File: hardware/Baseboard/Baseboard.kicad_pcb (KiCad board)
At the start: 2 copper layers, 160 x 160 mm, 77 parts, among them IC1 74HC00, IC10 W65C22, IC11 74HC148, IC12 74HC273, IC2 W65C02, IC3 74HC138, IC4 SYSTEM ROM, IC5 RAM, IC6 W65C22, IC7 W65C51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

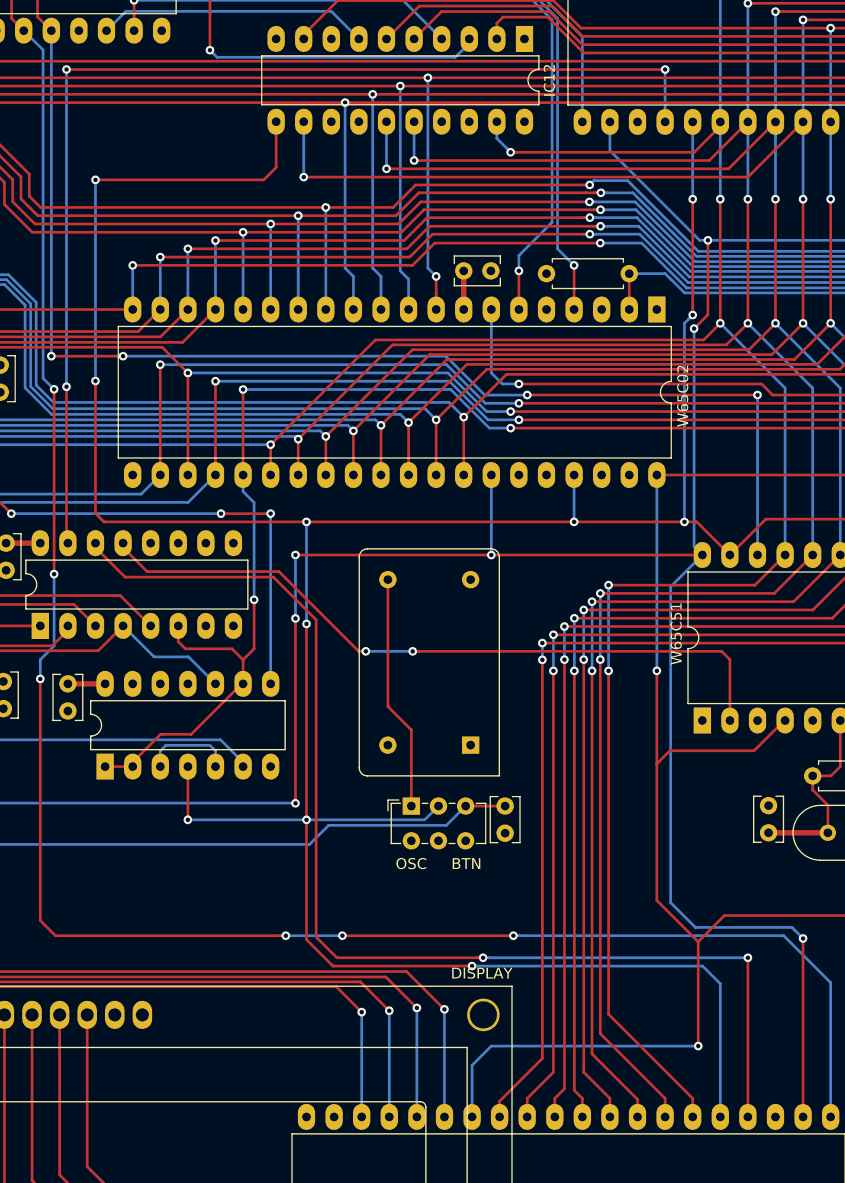
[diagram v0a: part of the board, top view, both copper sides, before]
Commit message: Move CS signals for peripheral devices to not(CS) pins
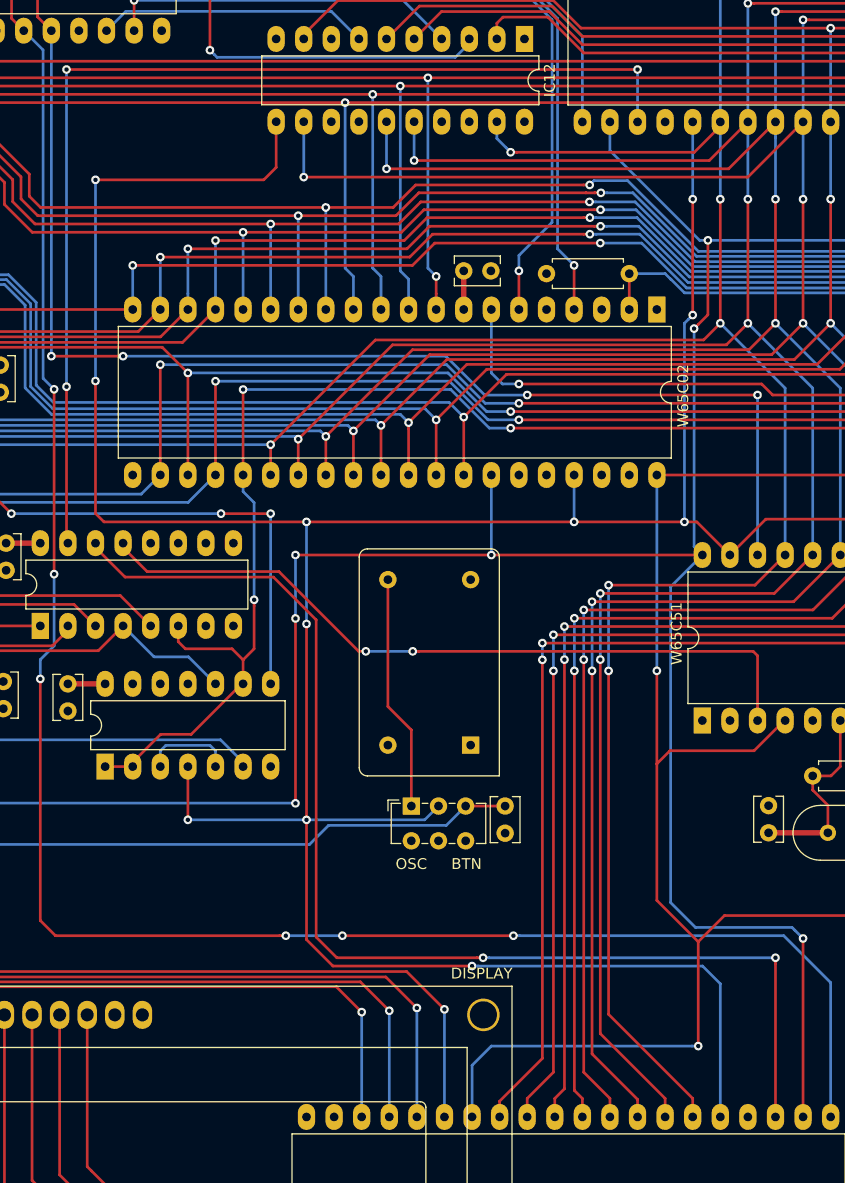
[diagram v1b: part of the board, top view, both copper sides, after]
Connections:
- IC10 pad 23: GND -> /Processor/~CS_VIA_2
- IC10 pad 24: /Processor/~CS_VIA_2 -> +5V
- IC6 pad 23: GND -> /Processor/~CS_VIA_1
- IC6 pad 24: /Processor/~CS_VIA_1 -> +5V
- IC7 pad 2: /Processor/~CS_ACIA -> +5V
- IC7 pad 3: GND -> /Processor/~CS_ACIA
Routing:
- net /Processor/~CS_ACIA: track 66.1 -> 68.9 mm
- net /Processor/~CS_VIA_2: track 107.9 -> 110.4 mm
- net /Processor/~CS_VIA_1: track 103.6 -> 101.1 mm
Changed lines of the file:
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@@
     (thickness 1.6)
     (drawings 17)
-    (tracks 1661)
+    (tracks 1662)
     (zones 0)
     (modules 77)
@@
       (net 10 /IO/PA3))
     (pad 24 thru_hole oval (at 15.24 40.64 270) (size 2.4 1.6) (drill 0.8) (layers *.Cu *.Mask)
-      (net 26 /Processor/~CS_VIA_1))
+      (net 2 +5V))
     (pad 4 thru_hole oval (at 0 7.62 270) (size 2.4 1.6) (drill 0.8) (layers *.Cu *.Mask)
       (net 9 /IO/PA2))
     (pad 23 thru_hole oval (at 15.24 43.18 270) (size 2.4 1.6) (drill 0.8) (layers *.Cu *.Mask)
-      (net 1 GND))
+      (net 26 /Processor/~CS_VIA_1))
     (pad 3 thru_hole oval (at 0 5.08 270) (size 2.4 1.6) (drill 0.8) (layers *.Cu *.Mask)
       (net 8 /IO/PA1))
@@
       (net 90 "/LCD / PS2/LCD6"))
     (pad 24 thru_hole oval (at 15.24 40.64 90) (size 2.4 1.6) (drill 0.8) (layers *.Cu *.Mask)
-      (net 52 /Processor/~CS_VIA_2))
+      (net 2 +5V))
     (pad 4 thru_hole oval (at 0 7.62 90) (size 2.4 1.6) (drill 0.8) (layers *.Cu *.Mask)
       (net 91 "/LCD / PS2/LCD5"))
     (pad 23 thru_hole oval (at 15.24 43.18 90) (size 2.4 1.6) (drill 0.8) (layers *.Cu *.Mask)
-      (net 1 GND))
+      (net 52 /Processor/~CS_VIA_2))
     (pad 3 thru_hole oval (at 0 5.08 90) (size 2.4 1.6) (drill 0.8) (layers *.Cu *.Mask)
       (net 92 "/LCD / PS2/LCD4"))
@@
       (net 80 /Processor/~ModemReady))
     (pad 3 thru_hole oval (at 0 5.08 90) (size 2.4 1.6) (drill 0.8) (layers *.Cu *.Mask)
-      (net 1 GND))
+      (net 31 /Processor/~CS_ACIA))
     (pad 16 thru_hole oval (at 15.24 30.48 90) (size 2.4 1.6) (drill 0.8) (layers *.Cu *.Mask)
       (net 96 /IO/~CarrierDetect))
     (pad 2 thru_hole oval (at 0 2.54 90) (size 2.4 1.6) (drill 0.8) (layers *.Cu *.Mask)
-      (net 31 /Processor/~CS_ACIA))
+      (net 2 +5V))
     (pad 15 thru_hole oval (at 15.24 33.02 90) (size 2.4 1.6) (drill 0.8) (layers *.Cu *.Mask)
       (net 2 +5V))
@@
   (segment (start 261.874 77.216) (end 255.194 70.536) (width 0.25) (layer F.Cu) (net 25) (status 10))
   (segment (start 255.194 70.536) (end 237.617 70.536) (width 0.25) (layer F.Cu) (net 25))
-  (via (at 244.094 87.63) (size 0.8) (drill 0.4) (layers F.Cu B.Cu) (net 26))
   (via (at 188.976 116.840048) (size 0.8) (drill 0.4) (layers F.Cu B.Cu) (net 26))
   (segment (start 188.976 131.115) (end 188.976 116.840048) (width 0.25) (layer F.Cu) (net 26) (status 10))
   (segment (start 189.103 131.242) (end 188.976 131.115) (width 0.25) (layer F.Cu) (net 26) (status 30))
   (via (at 188.976 87.63) (size 0.8) (drill 0.4) (layers F.Cu B.Cu) (net 26))
-  (segment (start 244.094 87.63) (end 188.976 87.63) (width 0.25) (layer F.Cu) (net 26))
-  (segment (start 244.094 92.456) (end 244.094 87.63) (width 0.25) (layer B.Cu) (net 26) (status 10))
   (segment (start 188.976 116.840048) (end 188.976 87.63) (width 0.25) (layer B.Cu) (net 26))
+  (segment (start 188.976 87.63) (end 241.554 87.63) (width 0.25) (layer F.Cu) (net 26))
+  (via (at 241.554 87.63) (size 0.8) (drill 0.4) (layers F.Cu B.Cu) (net 26))
+  (segment (start 241.554 87.63) (end 241.554 92.456) (width 0.25) (layer B.Cu) (net 26))
   (segment (start 280.1344 173.6468) (end 279.1316 172.644) (width 0.25) (layer F.Cu) (net 27))
   (segment (start 280.1344 174.7718) (end 280.1344 173.6468) (width 0.25) (layer F.Cu) (net 27) (status 10))
@@
   (segment (start 220.853 141.204) (end 216.535006 141.204) (width 0.25) (layer B.Cu) (net 31))
   (via (at 216.535 141.203994) (size 0.8) (drill 0.4) (layers F.Cu B.Cu) (net 31))
-  (segment (start 221.418685 141.204) (end 220.853 141.204) (width 0.25) (layer F.Cu) (net 31))
-  (segment (start 249.301 141.204) (end 221.418685 141.204) (width 0.25) (layer F.Cu) (net 31))
-  (segment (start 250.063 147.498) (end 250.063 141.966) (width 0.25) (layer F.Cu) (net 31) (status 10))
-  (segment (start 250.063 141.966) (end 249.301 141.204) (width 0.25) (layer F.Cu) (net 31))
   (segment (start 215.879994 141.203994) (end 216.535 141.203994) (width 0.25) (layer F.Cu) (net 31))
   (segment (start 208.534 133.858) (end 215.879994 141.203994) (width 0.25) (layer F.Cu) (net 31))
@@
   (segment (start 194.183 131.242) (end 194.183 131.642) (width 0.25) (layer F.Cu) (net 31) (status 30))
   (segment (start 194.183 131.642) (end 196.399 133.858) (width 0.25) (layer F.Cu) (net 31) (status 10))
+  (segment (start 221.418685 141.204) (end 220.853 141.204) (width 0.25) (layer F.Cu) (net 31))
+  (segment (start 252.202 141.204) (end 221.418685 141.204) (width 0.25) (layer F.Cu) (net 31))
+  (segment (start 252.603 147.574) (end 252.603 141.605) (width 0.25) (layer F.Cu) (net 31))
+  (segment (start 252.603 141.605) (end 252.202 141.204) (width 0.25) (layer F.Cu) (net 31))
   (segment (start 289.353521 172.143521) (end 290.0426 172.8326) (width 0.2) (layer F.Cu) (net 32) (status 20))
   (segment (start 286.502243 172.143521) (end 289.353521 172.143521) (width 0.2) (layer F.Cu) (net 32))
@@
   (segment (start 286.5505 158.9915) (end 287.465 159.906) (width 0.25) (layer F.Cu) (net 51))
   (via (at 227.33 169.418) (size 0.8) (drill 0.4) (layers F.Cu B.Cu) (net 52))
-  (segment (start 227.895685 169.418) (end 227.33 169.418) (width 0.25) (layer B.Cu) (net 52))
-  (segment (start 251.714 184.074) (end 251.714 169.418) (width 0.25) (layer F.Cu) (net 52) (status 10))
-  (segment (start 251.714 169.418) (end 227.895685 169.418) (width 0.25) (layer B.Cu) (net 52))
-  (via (at 251.714 169.418) (size 0.8) (drill 0.4) (layers F.Cu B.Cu) (net 52))
   (segment (start 226.764315 169.418) (end 227.33 169.418) (width 0.25) (layer F.Cu) (net 52))
   (segment (start 213.868 169.418) (end 226.764315 169.418) (width 0.25) (layer F.Cu) (net 52))
@@
   (segment (start 211.963 138.303) (end 211.963 167.513) (width 0.25) (layer F.Cu) (net 52))
   (segment (start 211.963 167.513) (end 213.868 169.418) (width 0.25) (layer F.Cu) (net 52))
+  (segment (start 227.33 169.418) (end 227.895685 169.418) (width 0.25) (layer B.Cu) (net 52))
+  (via (at 254.254 169.418) (size 0.8) (drill 0.4) (layers F.Cu B.Cu) (net 52))
+  (segment (start 227.895685 169.418) (end 254.254 169.418) (width 0.25) (layer B.Cu) (net 52))
+  (segment (start 254.254 169.983685) (end 254.254 184.074) (width 0.25) (layer F.Cu) (net 52))
+  (segment (start 254.254 169.418) (end 254.254 169.983685) (width 0.25) (layer F.Cu) (net 52))
   (segment (start 228.473 124.9495) (end 228.34 125.0825) (width 0.25) (layer B.Cu) (net 53) (status 30))
   (segment (start 228.34 125.0825) (end 228.34 124.6825) (width 0.25) (layer F.Cu) (net 53) (status 30))

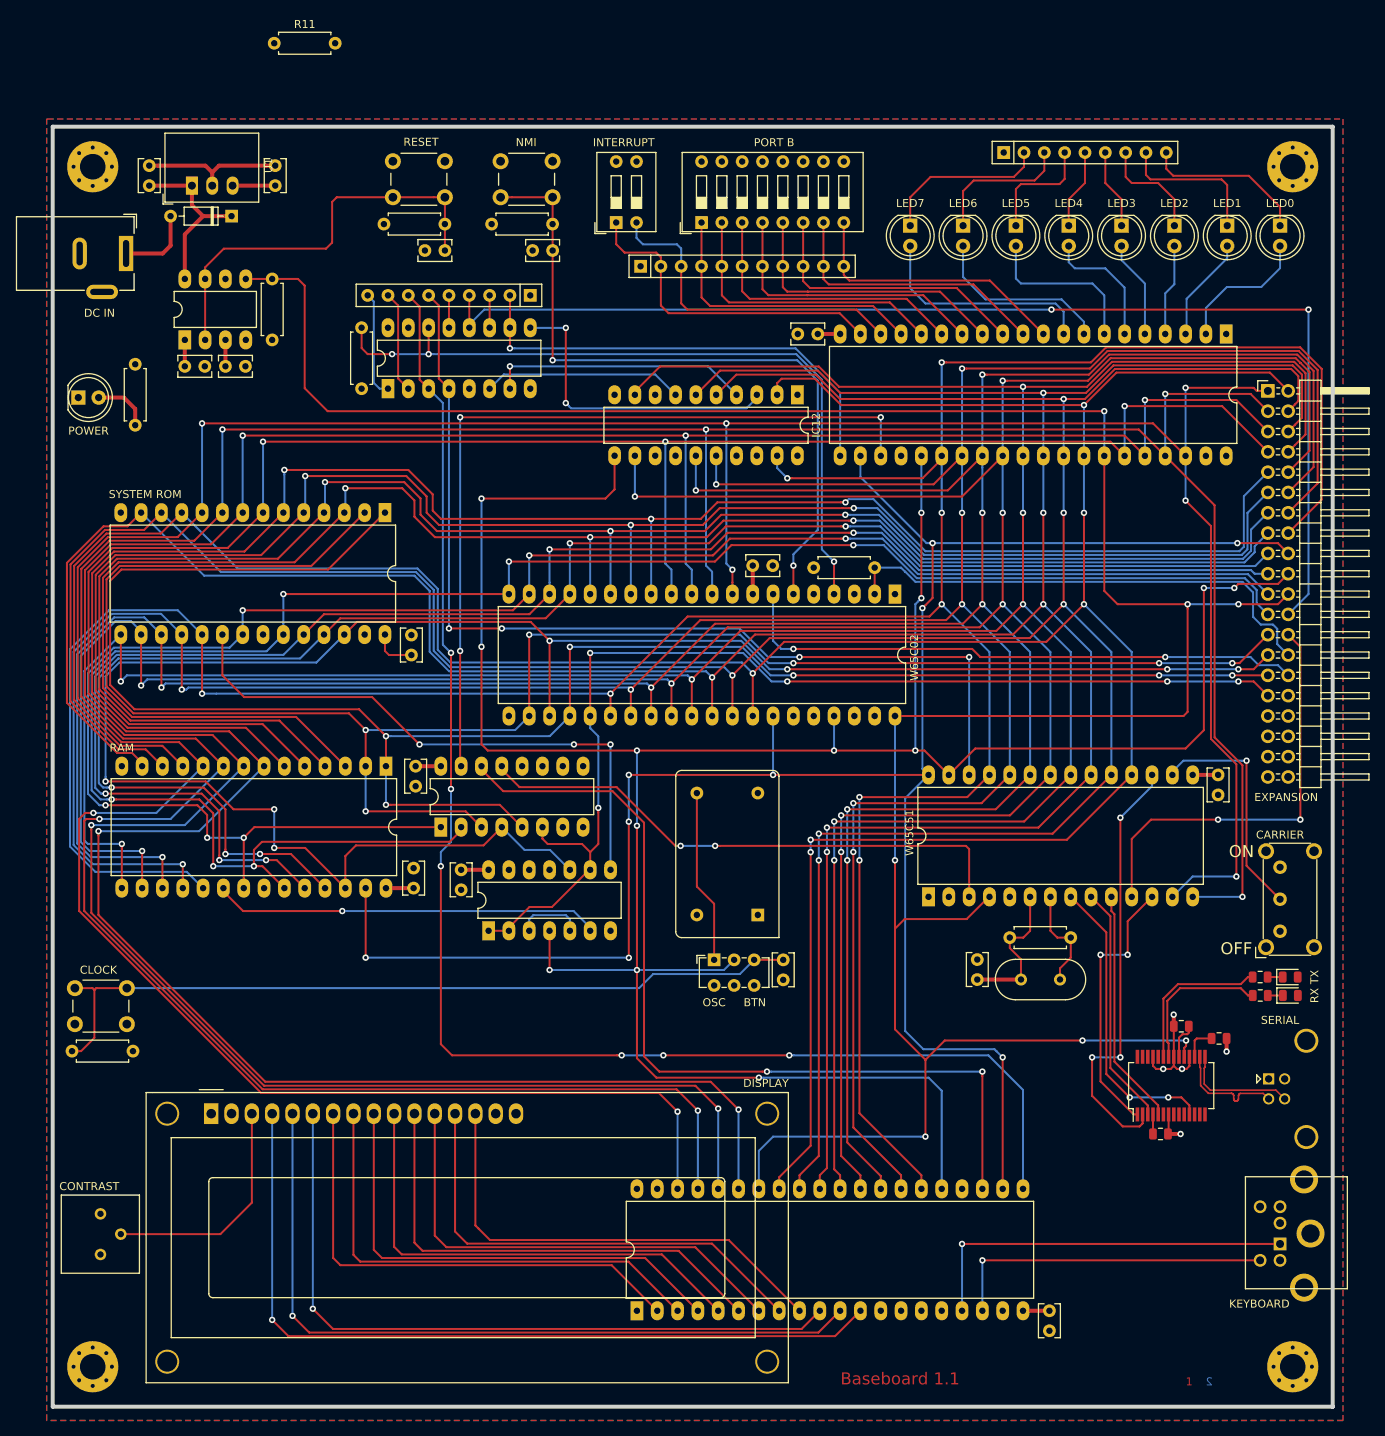
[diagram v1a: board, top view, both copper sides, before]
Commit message: Add VP signal to expansion header, optimize routing
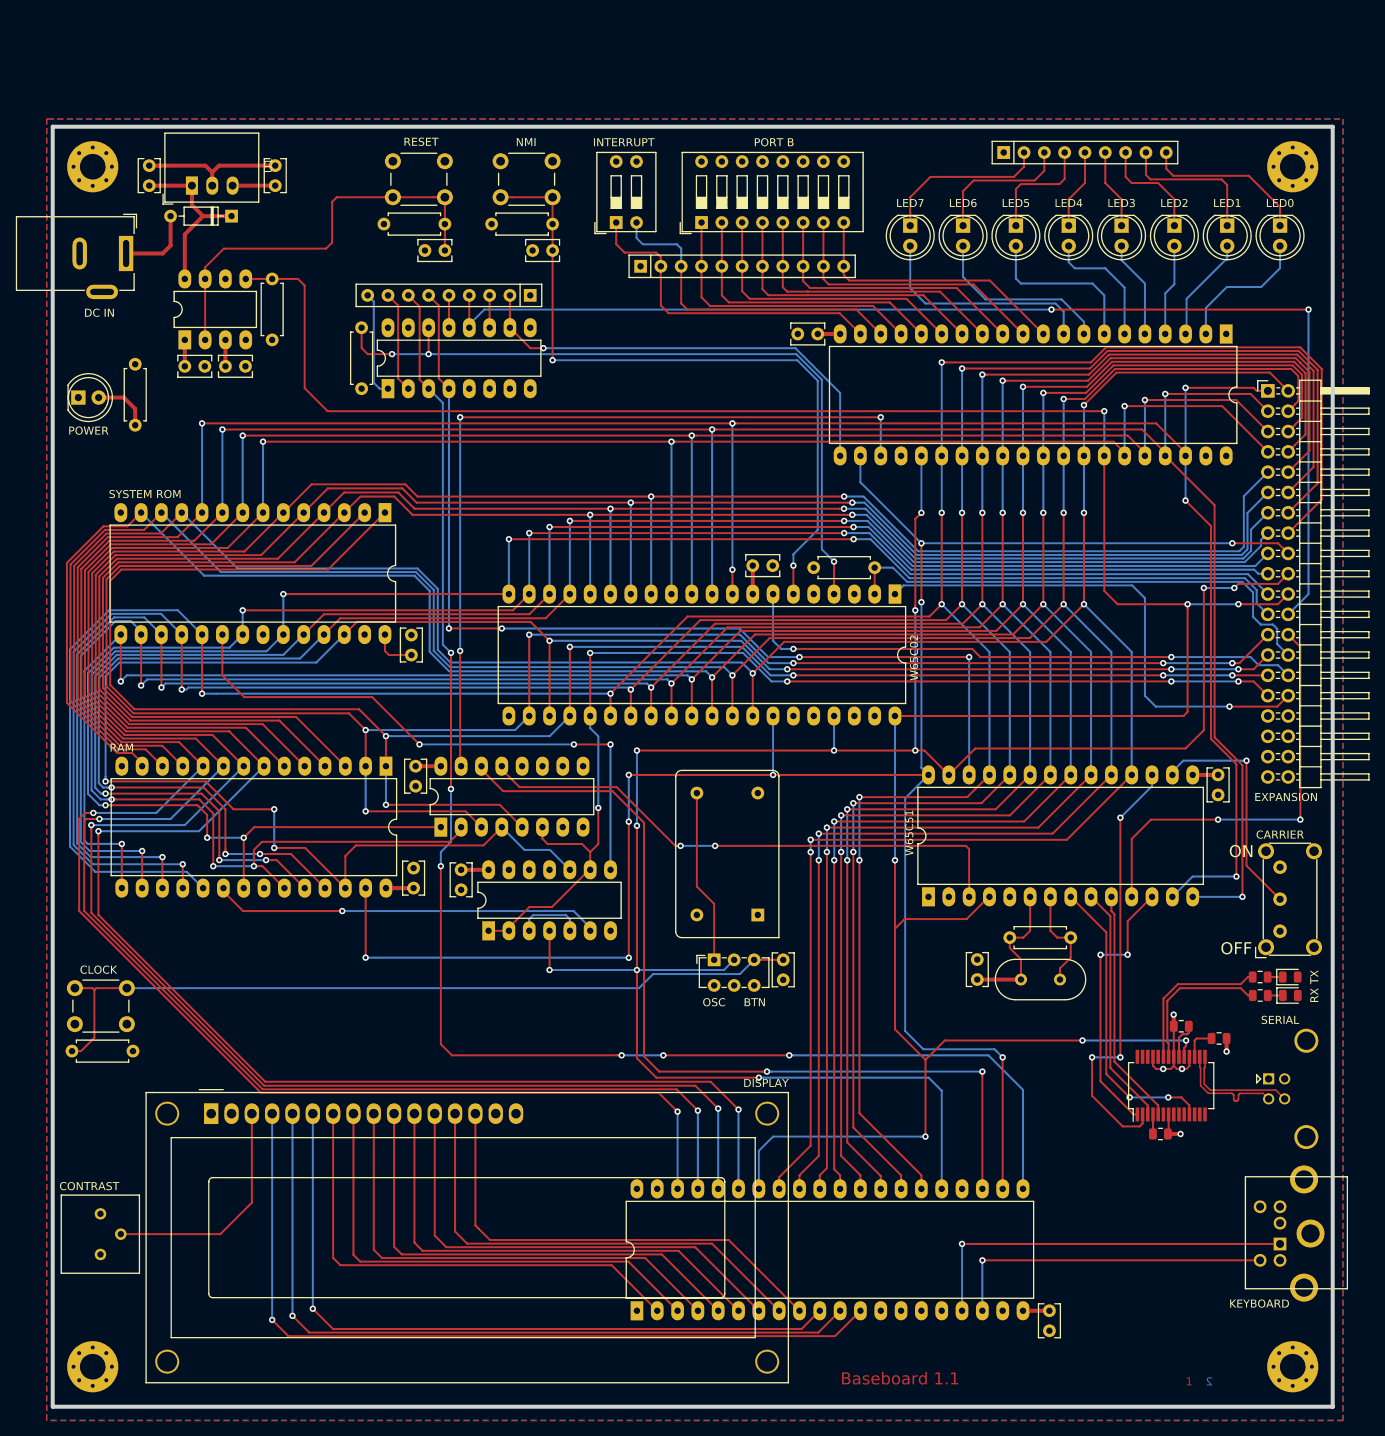
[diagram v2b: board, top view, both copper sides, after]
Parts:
- removed IC12: 74HC273, Package_DIP:DIP-20_W7.62mm_LongPads
- removed R11: 10k, Resistor_THT:R_Axial_DIN0207_L6.3mm_D2.5mm_P7.62mm_Horizontal
- RN2: value 470 -> 390
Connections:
- IC11 pad 6: Net-(IC11-Pad6) -> (no net)
- IC11 pad 7: Net-(IC11-Pad7) -> (no net)
- IC11 pad 9: Net-(IC11-Pad9) -> (no net)
- IC2 pad 1: (no net) -> /IO/~VP
- X3 pad 32: (no net) -> /IO/~VP
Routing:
- net /IO/Clock: track 336.3 -> 264.6 mm, vias 13 -> 11
- net /IO/~VP: track 0.00 -> 63.6 mm, vias 0 -> 1
- net /IO/D4: track 404.1 -> 350.9 mm, vias 9 -> 8
- net /IO/D3: track 394.0 -> 342.7 mm
- net /IO/D2: track 396.0 -> 350.1 mm
- net /IO/D1: track 396.8 -> 351.1 mm
- net /IO/D5: track 397.7 -> 355.8 mm, vias 9 -> 8
- net /IO/D0: track 391.5 -> 350.1 mm
- net Net-(IC11-Pad9): track 38.9 -> 0.00 mm, vias 2 -> 0
- net /IO/D6: track 397.1 -> 361.3 mm, vias 9 -> 8
- net Net-(IC11-Pad7): track 32.6 -> 0.00 mm, vias 1 -> 0
- net Net-(IC11-Pad6): track 25.0 -> 0.00 mm
- net /IO/D7: track 389.7 -> 365.7 mm, vias 8 -> 7
- net /IO/A4: track 222.6 -> 217.8 mm, vias 3 -> 2
- net /IO/A5: track 220.2 -> 216.3 mm, vias 3 -> 2
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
